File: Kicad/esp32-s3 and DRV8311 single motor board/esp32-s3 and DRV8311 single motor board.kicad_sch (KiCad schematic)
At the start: 65 parts, among them J1 JST SH SM04B, J2 7 pin FPC 0.3mm, J4 Conn_01x02_Pin, SW1 SW_Push, SW2 SW_Push, U5 ESP32-S3, U6 74HC595, Y1 40mhz, 10ppm

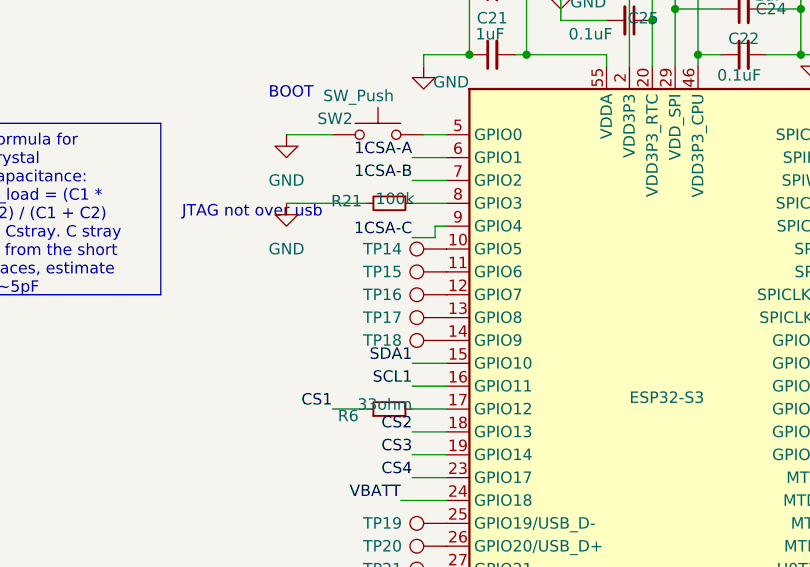
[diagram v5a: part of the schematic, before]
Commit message: Routing test pads & power
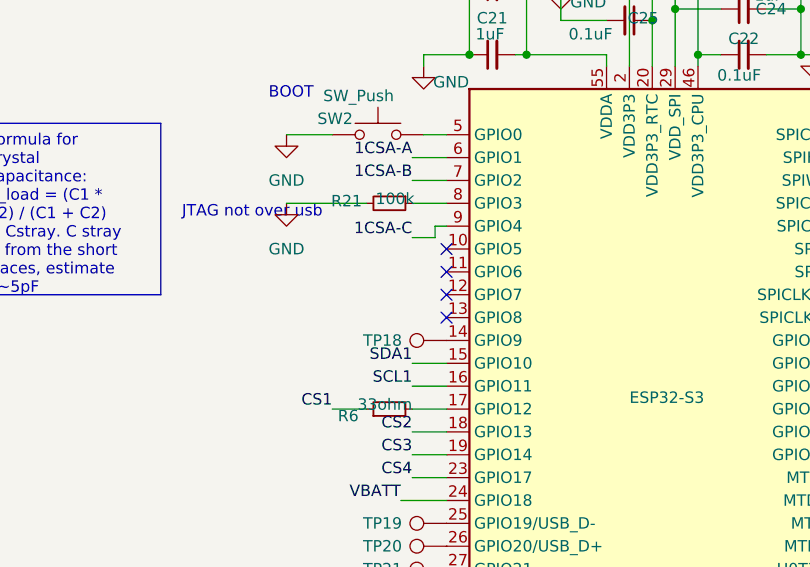
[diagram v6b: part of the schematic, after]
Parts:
- removed TP14, TP15, TP16, TP17: ~, TestPoint:TestPoint_Pad_D1.0mm, symbol Connector:TestPoint
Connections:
- no-connect marks 12 -> 16

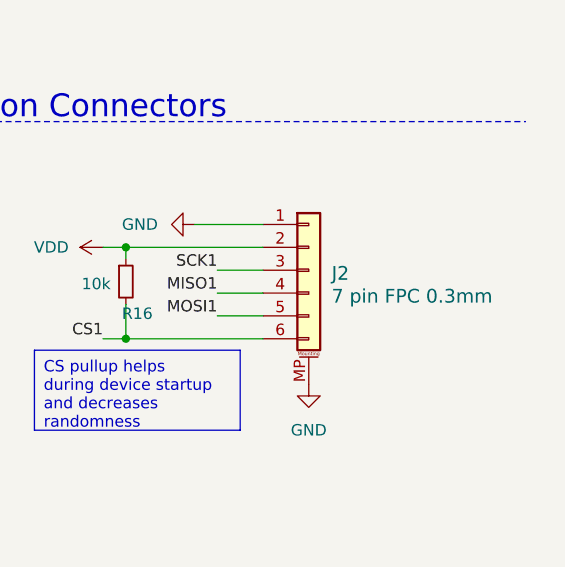
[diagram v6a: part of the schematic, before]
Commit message: Added 7 pin FPC connector footprint
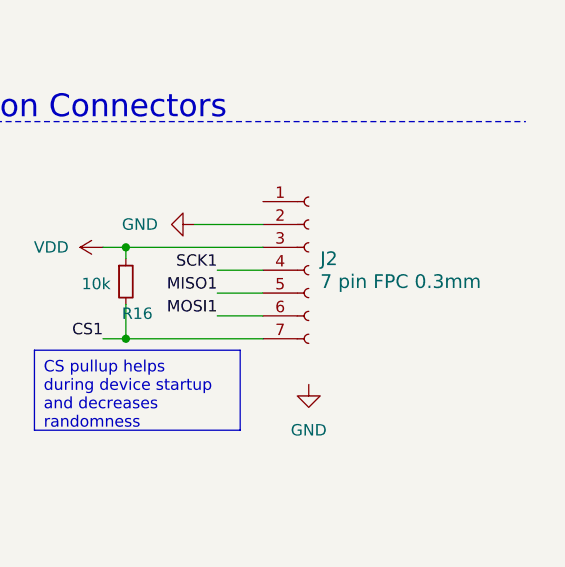
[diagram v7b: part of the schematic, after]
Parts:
- J2: footprint Connector_JST:JST_SH_SM06B-SRSS-TB_1x06-1MP_P1.00mm_Horizontal -> custom_Interface_HID:fpc_7pin_0.3mm_connector Panasonic; symbol Connector_Generic_MountingPin:Conn_01x06_MountingPin -> Connector:Conn_01x07_Socket
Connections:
- net CS1: now also J2.7 (Pin_7); no longer J2.6 (Pin_6)
- net GND: now also J2.2 (Pin_2); no longer J2.1 (Pin_1), J2.MP (MountPin)
- net MISO1: now also J2.5 (Pin_5); no longer J2.4 (Pin_4)
- net MOSI1: now also J2.6 (Pin_6); no longer J2.5 (Pin_5)
- net SCK1: now also J2.4 (Pin_4); no longer J2.3 (Pin_3)
- net VDD: now also J2.3 (Pin_3); no longer J2.2 (Pin_2)
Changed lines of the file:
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@@
 	)
 	(symbol
-		(lib_id "Connector_Generic_MountingPin:Conn_01x06_MountingPin")
+		(lib_id "Connector:Conn_01x07_Socket")
 		(at 260.35 90.17 0)
 		(unit 1)
@@
 		(fields_autoplaced yes)
 		(property "Reference" "J2"
-			(at 262.89 90.5255 0)
+			(at 261.62 88.8999 0)
 			(effects
 				(font
@@
 		)
 		(property "Value" "7 pin FPC 0.3mm"
-			(at 262.89 93.0655 0)
+			(at 261.62 91.4399 0)
 			(effects
 				(font
@@
 			)
 		)
-		(property "Footprint" "Connector_JST:JST_SH_SM06B-SRSS-TB_1x06-1MP_P1.00mm_Horizontal"
+		(property "Footprint" "custom_Interface_HID:fpc_7pin_0.3mm_connector Panasonic"
 			(at 260.35 90.17 0)
 			(effects
@@
 			)
 		)
-		(property "Description" "Generic connectable mounting pin connector, single row, 01x06, script generated (kicad-library-utils/schlib/autogen/connector/)"
+		(property "Description" "Generic connector, single row, 01x07, script generated"
 			(at 260.35 90.17 0)
 			(effects
@@
 		(pin "5"
 		)
-		(pin "MP"
+		(pin "7"
 		)
 		(instances

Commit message: Finished routing everything
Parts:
- removed J4: Conn_01x02_Pin, Connector_PinHeader_2.54mm:PinHeader_1x02_P2.54mm_Vertical, symbol Connector:Conn_01x02_Pin
- removed TP13, TP2, TP3, TP4, TP5: TestPoint, TestPoint:TestPoint_Pad_D1.0mm, symbol Connector:TestPoint
- added TP14, TP15: TestPoint, TestPoint:TestPoint_Pad_D1.0mm, symbol Connector:TestPoint
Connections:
- net CS1: now also J2.5 (Pin_5); no longer J2.7 (Pin_7)
- net GND: now also J2.3 (Pin_3), J2.7 (Pin_7); no longer J2.2 (Pin_2)
- net MISO1: now also J2.4 (Pin_4); no longer J2.5 (Pin_5)
- net SCK1: now also J2.2 (Pin_2); no longer J2.4 (Pin_4)
- net UART0_RX: now also TP14.1
- net UART0_TX: now also TP15.1
- net VDD: now also J2.1 (Pin_1); no longer J2.3 (Pin_3)
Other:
- note added: "DEBUG pins. Access SPI via magnetic sensor header"
- note removed: "DEBUG pins"
- moved on the sheet: R16
